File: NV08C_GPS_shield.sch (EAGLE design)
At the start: 46 parts, among them IC1 74LVC1T45SOT23-HAND, IC2 74LVC1T45SOT23-HAND, IC3 74LVC1T45SOT23-HAND, IC4 74LVC1T45SOT23-HAND, IC5 74LVC1T45SOT23-HAND, IC6 74LVC1T45SOT23-HAND, IC7 MCP1702-3.3, X1 CONN-SMATHD-SMD-EDGE

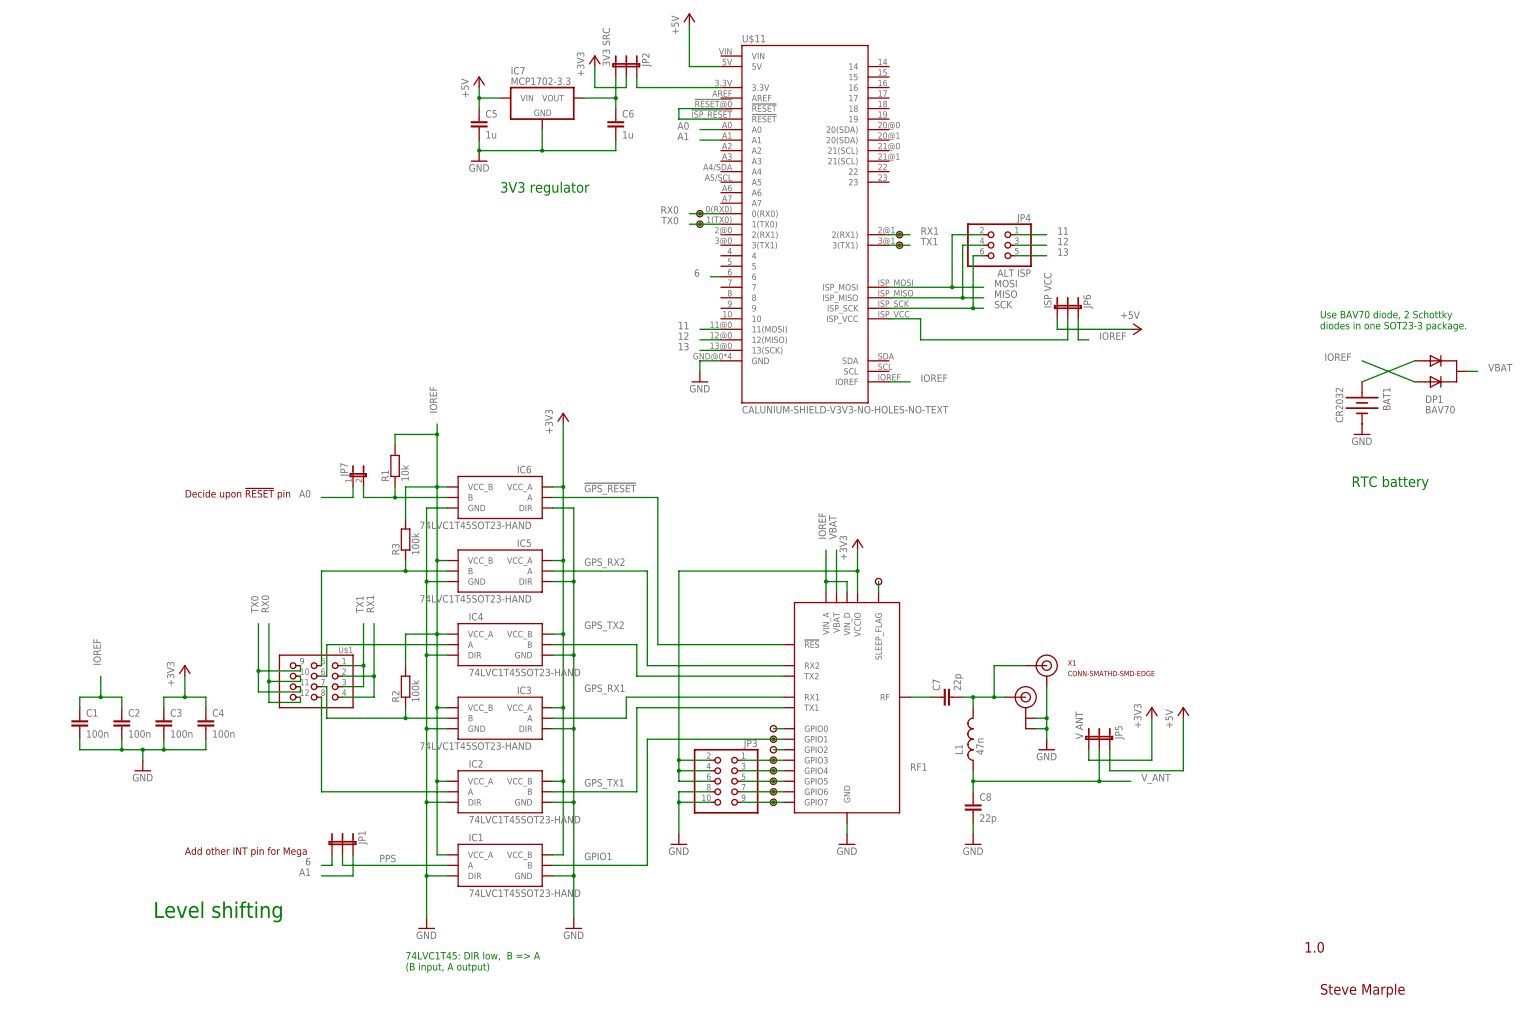
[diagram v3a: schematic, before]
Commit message: Adding protection resistors in GPS TX lines.
Enables the same UART to be used to access the bootloader during the boot
sequence without damaging the level shifters or external FTDI device.
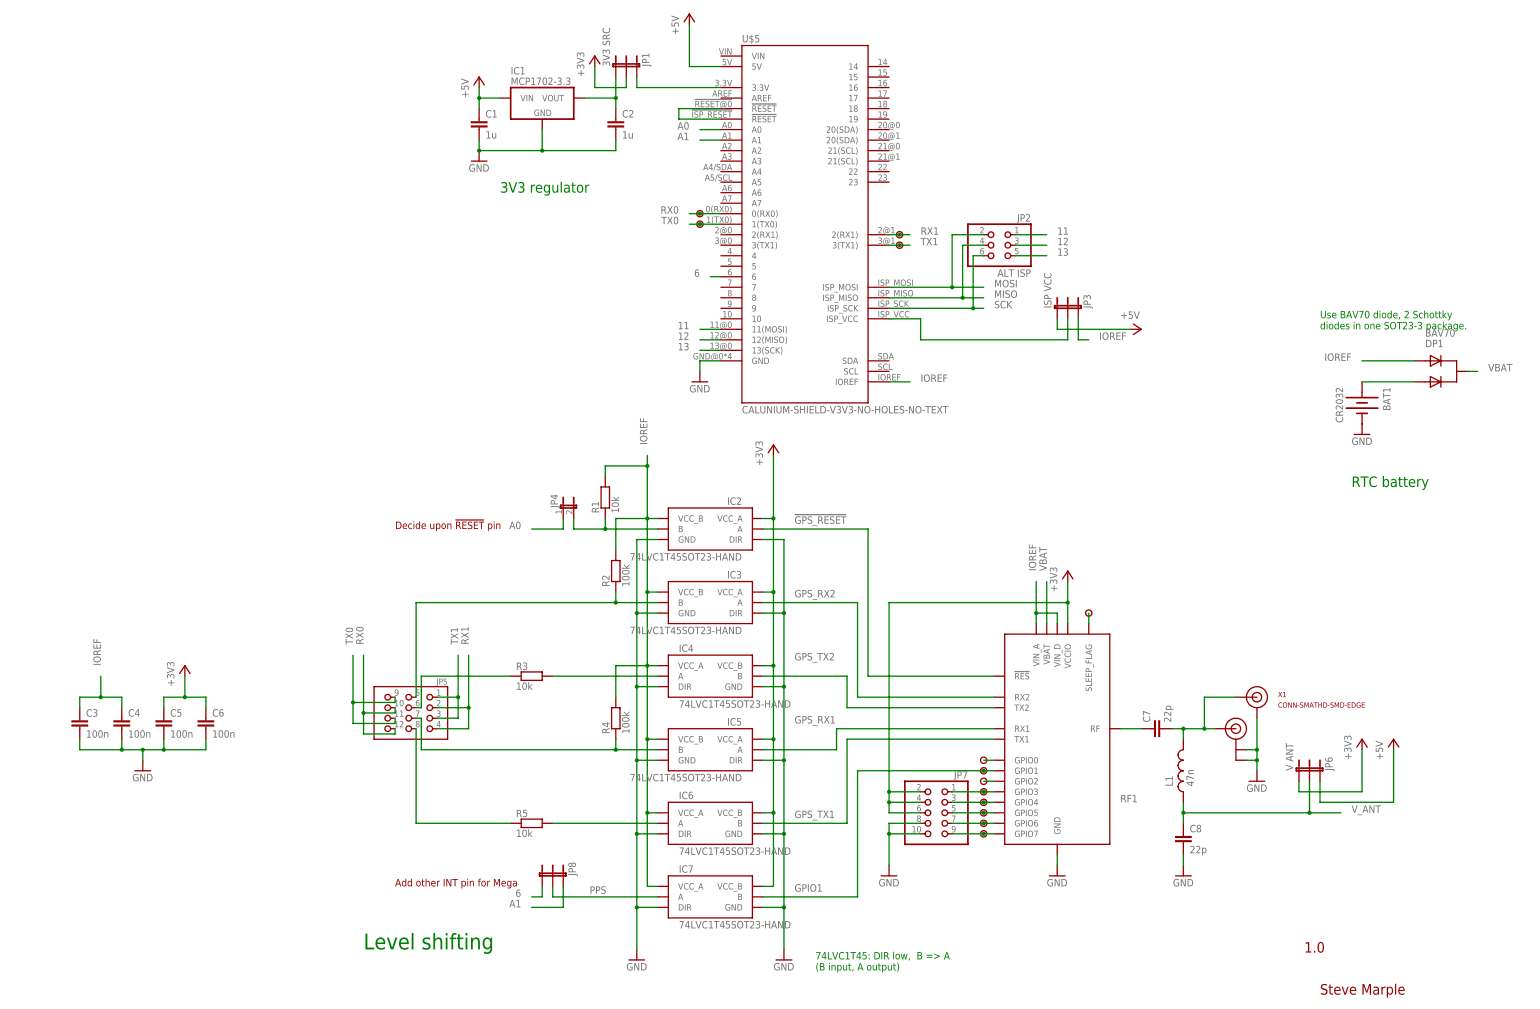
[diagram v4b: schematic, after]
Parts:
- removed U$16, U$17: PAD, SteveMarple:PAD
- added JP8: JUMPER-3PTH, SparkFun:JUMPER-3PTH
- added R4: 100k, SteveMarple:RESISTOR1206-HAND
- added R5: 10k, SteveMarple:RESISTOR1206-HAND
- added U$2: PAD, SteveMarple:PAD
- C1, C2: value 100n -> 1u
- C5, C6: value 1u -> 100n
- IC1: value 74LVC1T45SOT23-HAND -> MCP1702-3.3; device SteveMarple:74LVC1T45SOT23-HAND -> SteveMarple:MCP1702
- IC7: value MCP1702-3.3 -> 74LVC1T45SOT23-HAND; device SteveMarple:MCP1702 -> SteveMarple:74LVC1T45SOT23-HAND
- JP1: value JUMPER-3PTH -> 3V3 SRC
- JP2: value 3V3 SRC -> ALT ISP; device SparkFun:JUMPER-3PTH -> pinhead:PINHD-2X3
- JP3: value (none) -> ISP VCC; device pinhead:PINHD-2X5 -> SparkFun:JUMPER-3PTH
- JP4: value ALT ISP -> (none); device pinhead:PINHD-2X3 -> SparkFun:JUMPER-2PTH
- JP5: value V ANT -> PIN_3X4; device SparkFun:JUMPER-3PTH -> pinhead_3row:PIN_3X4
- JP6: value ISP VCC -> V ANT
- JP7: device SparkFun:JUMPER-2PTH -> pinhead:PINHD-2X5
- R1: device SteveMarple:RESISTOR0805-HAND -> SteveMarple:RESISTOR1206-HAND
- R3: value 100k -> 10k
- U$1: value PIN_3X4 -> PAD; device pinhead_3row:PIN_3X4 -> SteveMarple:PAD
- U$10: value PAD -> ?
- U$11: value CALUNIUM-SHIELD-V3V3-NO-HOLES-NO-TEXT -> PAD; device SteveMarple:CALUNIUM-SHIELD-V3V3-NO-HOLES-NO-TEXT -> SteveMarple:PAD
- U$13: value U.FL -> PAD; device SparkFun:U.FL -> SteveMarple:PAD
- U$5: value PAD -> CALUNIUM-SHIELD-V3V3-NO-HOLES-NO-TEXT; device SteveMarple:PAD -> SteveMarple:CALUNIUM-SHIELD-V3V3-NO-HOLES-NO-TEXT
- U$7: value PAD -> U.FL; device SteveMarple:PAD -> SparkFun:U.FL
- U$8: value ? -> PAD
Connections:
- new net N$3: IC4.A, R3.2
- new net N$5: IC6.A, R5.2
- net !GPS_RESET: now also IC2.A; no longer IC6.A
- net +3V3: now also C5.1, C6.1, IC2.VCC_A, IC6.VCC_B, IC7.VCC_B, JP1.2, JP6.3, JP7.2, JP7.4, JP7.6; no longer C3.1, C4.1, IC1.VCC_B, IC2.VCC_B, IC6.VCC_A, JP2.2, JP3.2, JP3.4, JP3.6, JP5.3
- net +5V: now also C1.1, IC1.VIN, JP3.3, JP6.1, U$5.5V; no longer C5.1, IC7.VIN, JP5.1, JP6.3, U$11.5V
- net 11: now also JP2.1, U$5.11(MOSI); no longer JP4.1, U$11.11(MOSI)
- net 12: now also JP2.3, U$5.12(MISO); no longer JP4.3, U$11.12(MISO)
- net 13: now also JP2.5, U$5.13(SCK); no longer JP4.5, U$11.13(SCK)
- net 3V3_SHIELD: now also JP1.1, U$5.3.3V; no longer JP2.1, U$11.3.3V
- net 6: now also JP8.3, U$5.6; no longer JP1.3, U$11.6
- net A0: now also JP4.1, U$5.A0; no longer JP7.1, U$11.A0
- net A1: now also JP8.1, U$5.A1; no longer JP1.1, U$11.A1
- net GND: now also IC7.DIR, JP7.10, JP7.8, U$5.GND, U$7.GND@0, U$7.GND@1; no longer IC1.DIR, JP3.10, JP3.8, U$11.GND, U$13.GND@0, U$13.GND@1
- net GPIO0: now also U$8.1; no longer U$10.1
- net GPIO1: now also IC7.B; no longer IC1.B
- net GPIO2: now also U$10.1; no longer U$8.1
- net GPIO3: now also JP7.1, U$11.1; no longer JP3.1, U$7.1
- net GPIO4: now also JP7.3, U$12.1; no longer JP3.3, U$6.1
- net GPIO5: now also JP7.5, U$13.1; no longer JP3.5, U$5.1
- net GPIO6: now also JP7.7, U$14.1; no longer JP3.7, U$4.1
- net GPIO7: now also JP7.9, U$15.1; no longer JP3.9, U$3.1
- net GPS_RX1: now also IC5.A; no longer IC3.A
- net GPS_RX2: now also IC3.A; no longer IC5.A
- net GPS_TX1: now also IC6.B; no longer IC2.B
- net IOREF: now also C3.1, C4.1, IC2.VCC_B, IC6.VCC_A, IC7.VCC_A, JP3.1, R4.2, U$5.IOREF; no longer C1.1, C2.1, IC1.VCC_A, IC2.VCC_A, IC6.VCC_B, JP6.1, R3.2, U$11.IOREF
- net ISP_VCC: now also JP3.2, U$5.ISP_VCC; no longer JP6.2, U$11.ISP_VCC
- net MISO: now also JP2.4, U$5.ISP_MISO; no longer JP4.4, U$11.ISP_MISO
- net MOSI: now also JP2.2, U$5.ISP_MOSI; no longer JP4.2, U$11.ISP_MOSI
- net N$1: now also C2.1, IC1.VOUT, JP1.3; no longer C6.1, IC7.VOUT, JP2.3
- net N$12: now also IC5.B, JP5.7, R4.1; no longer IC3.B, R2.1, U$1.7
- net N$13: now also JP5.6, R3.1; no longer IC4.A, U$1.6
- net N$15: now also JP5.8, R5.1; no longer IC2.A, U$1.8
- net N$2: now also U$5.!RESET@0, U$5.!RESET@1; no longer U$11.!RESET@0, U$11.!RESET@1
- net N$20: now also U$6.1; no longer U$12.1
- net N$4: now also U$7.SIGNAL; no longer U$13.SIGNAL
- net N$6: now also IC3.B, JP5.5, R2.1; no longer IC5.B, R3.1, U$1.5
- net N$8: now also IC2.B, JP4.2; no longer IC6.B, JP7.2
- net PPS: now also IC7.A, JP8.2; no longer IC1.A, JP1.2
- net RX0: now also JP5.10, JP5.12, U$1.1, U$5.0(RX0); no longer U$1.10, U$1.12, U$11.0(RX0), U$14.1
- net RX1: now also JP5.2, JP5.4, U$3.1, U$5.2(RX1)@1; no longer U$1.2, U$1.4, U$11.2(RX1)@1, U$16.1
- net SCK: now also JP2.6, U$5.ISP_SCK; no longer JP4.6, U$11.ISP_SCK
- net TX0: now also JP5.11, JP5.9, U$2.1, U$5.1(TX0); no longer U$1.11, U$1.9, U$11.1(TX0), U$15.1
- net TX1: now also JP5.1, JP5.3, U$4.1, U$5.3(TX1)@1; no longer U$1.1, U$1.3, U$11.3(TX1)@1, U$17.1
- net V_ANT: now also JP6.2; no longer JP5.2
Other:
- moved on the sheet: C1, C2, C3, C4, C5, C6, C7, C8, DP1, IC2, IC3, IC4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

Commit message: Change PPS pin used. Add decoupling for NV08C module.
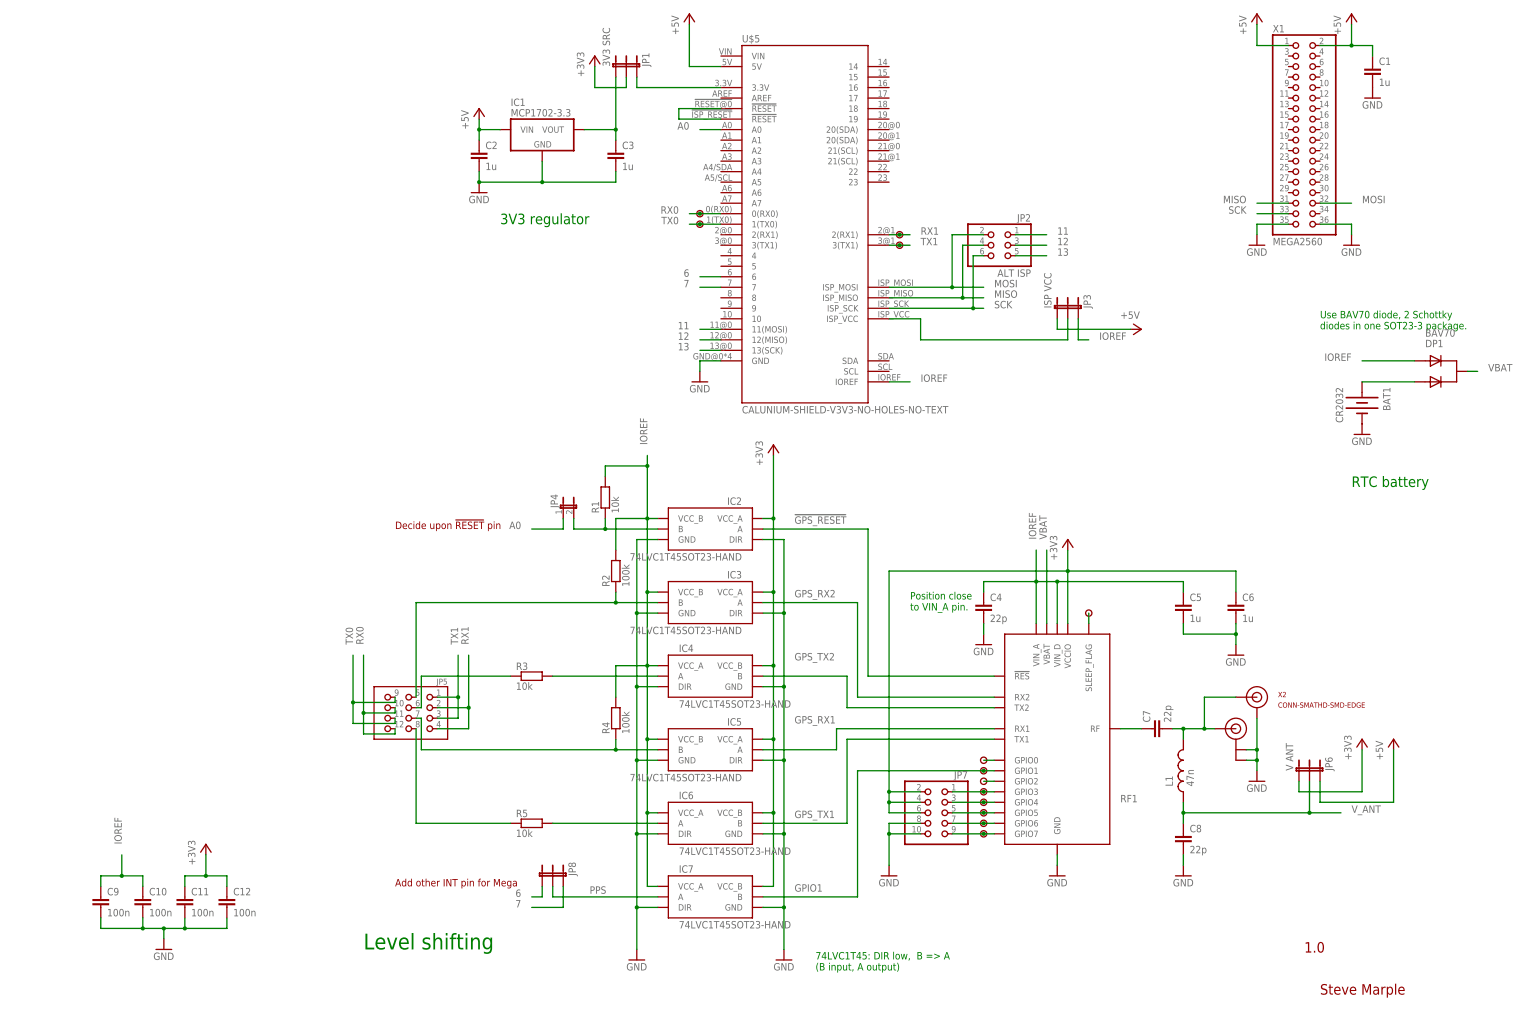
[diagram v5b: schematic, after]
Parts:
- added C10, C11, C12, C9: 100n, SteveMarple:C-EU1206-HAND
- added X2: CONN-SMATHD-SMD-EDGE, SteveMarple:CONN-SMATHD-SMD-EDGE
- C3, C5, C6: value 100n -> 1u
- C4: value 100n -> 22p; device SteveMarple:C-EU1206-HAND -> SteveMarple:C-EU0805-HAND
- X1: value CONN-SMATHD-SMD-EDGE -> MEGA2560; device SteveMarple:CONN-SMATHD-SMD-EDGE -> pinhead:PINHD-2X18
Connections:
- removed net A1: JP8.1, U$5.A1
- new net 7: JP8.1, U$5.7
- net +3V3: now also C11.1, C12.1; no longer C5.1
- net +5V: now also C2.1, X1.1, X1.2
- net GND: now also C10.2, C11.2, C12.2, C9.2, X1.35, X1.36, X2.GND; no longer X1.GND
- net IOREF: now also C10.1, C5.1, C9.1; no longer C3.1
- net MISO: now also X1.31
- net MOSI: now also X1.32
- net N$1: now also C3.1; no longer C2.1
- net N$4: now also X2.SIGNAL; no longer X1.SIGNAL
- net SCK: now also X1.33
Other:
- note added: "Position close to VIN_A pin."
- moved on the sheet: C1, C2, C3, C4, C5, C6, IC1

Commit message: Minor layout and silkscreen fixes.
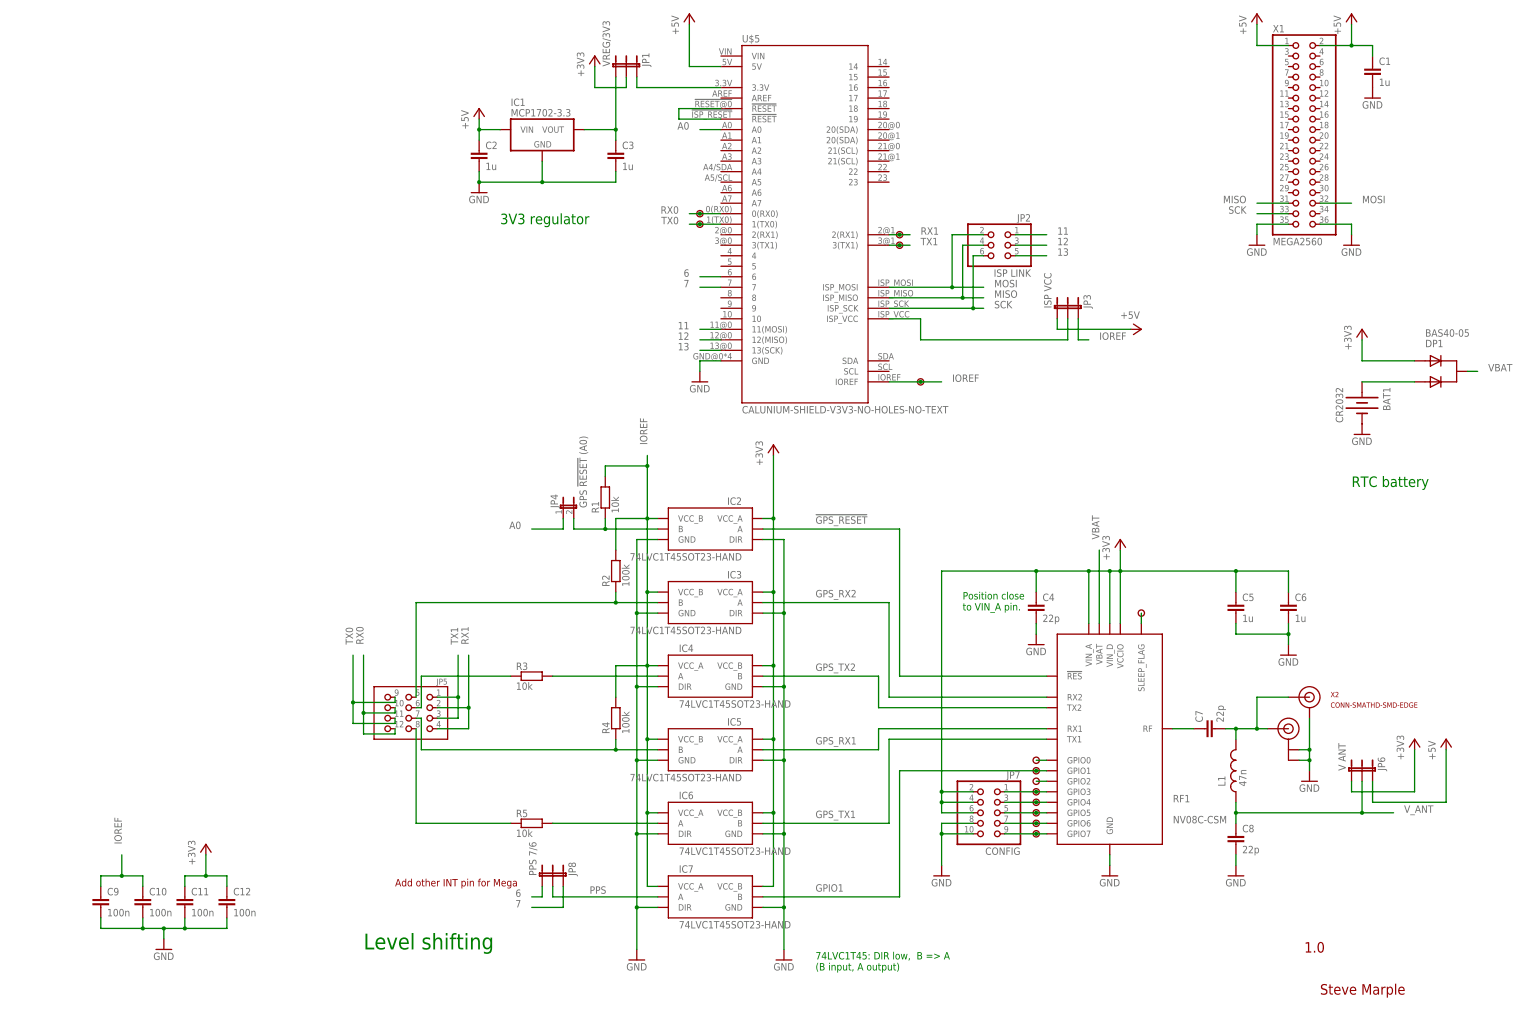
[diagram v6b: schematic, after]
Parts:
- added X3: U.FL, SparkFun:U.FL
- DP1: value BAV70 -> BAS40-05
- JP1: value 3V3 SRC -> VREG/3V3
- JP2: value ALT ISP -> ISP LINK
- JP4: value (none) -> GPS !RESET! (A0)
- JP7: value (none) -> CONFIG
- JP8: value JUMPER-3PTH -> PPS 7/6
- RF1: value (none) -> NV08C-CSM
- U$7: value U.FL -> PAD; device SparkFun:U.FL -> SteveMarple:PAD
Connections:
- net N$12 renamed GPS_RX1_IOREF
- net N$13 renamed GPS_TX2_IOREF
- net N$15 renamed GPS_TX1_IOREF
- net N$2 renamed !RESET
- net N$6 renamed GPS_RX2_IOREF
- net +3V3: now also C4.1, C5.1, DP1.A2, RF1.VIN_A, RF1.VIN_D
- net GND: now also X3.GND@0, X3.GND@1; no longer U$7.GND@0, U$7.GND@1
- net IOREF: now also U$6.1; no longer C4.1, C5.1, DP1.A2, RF1.VIN_A, RF1.VIN_D
- net N$20: now also U$7.1; no longer U$6.1
- net N$4: now also X3.SIGNAL; no longer U$7.SIGNAL
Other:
- note removed: "Decide upon !RESET! pin"
- note removed: "Use BAV70 diode, 2 Schottky diodes in one SOT23-3 package."
- moved on the sheet: C4, C5, C6, C7, C8, JP6, JP7, L1, RF1, X2
